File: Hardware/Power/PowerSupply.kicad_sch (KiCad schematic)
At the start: 23 parts, among them U1 ADC104S021

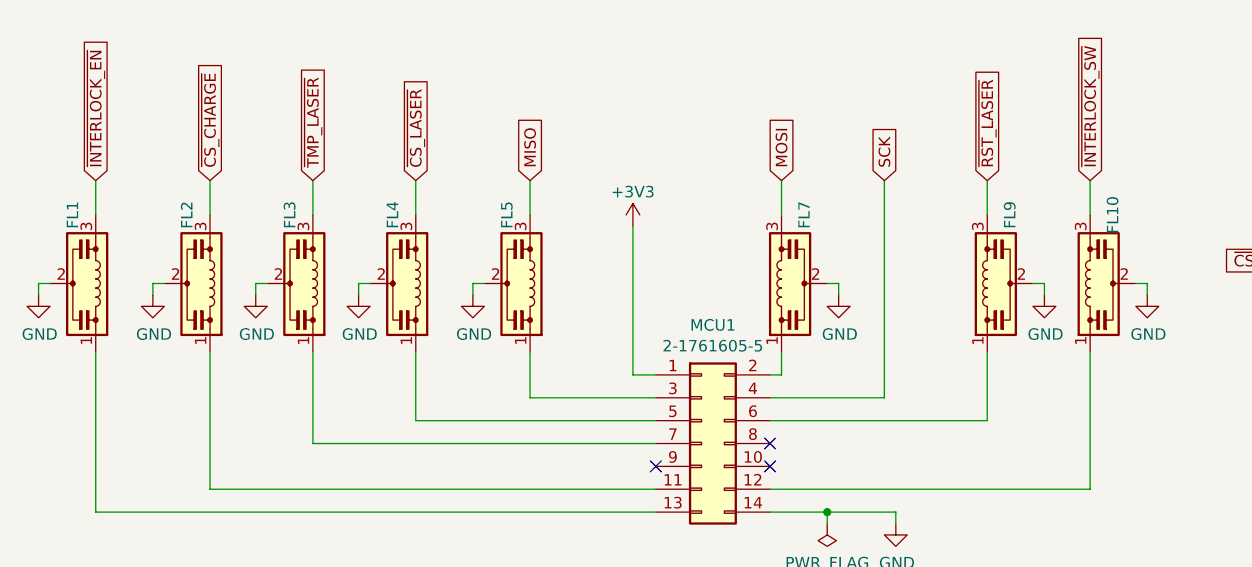
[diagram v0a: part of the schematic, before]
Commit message: Update to kicad 8
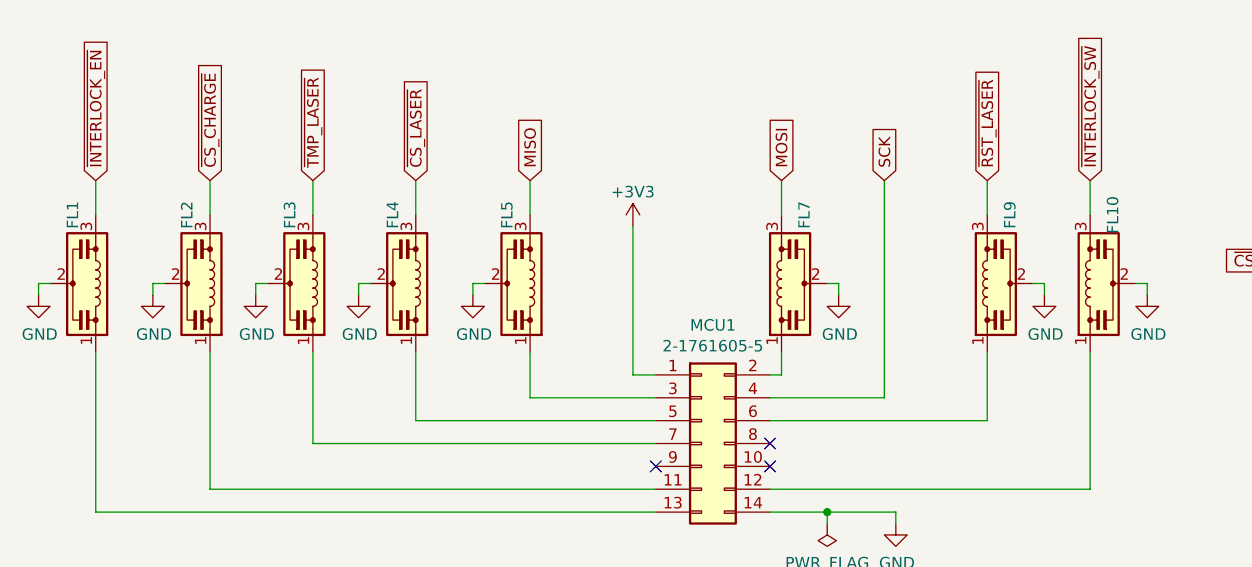
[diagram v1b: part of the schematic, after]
